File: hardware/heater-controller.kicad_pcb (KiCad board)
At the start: 2 copper layers, 65 x 63 mm, 12 parts, among them J1 Vitotronic plug 96, Q1 SFH 309 FA

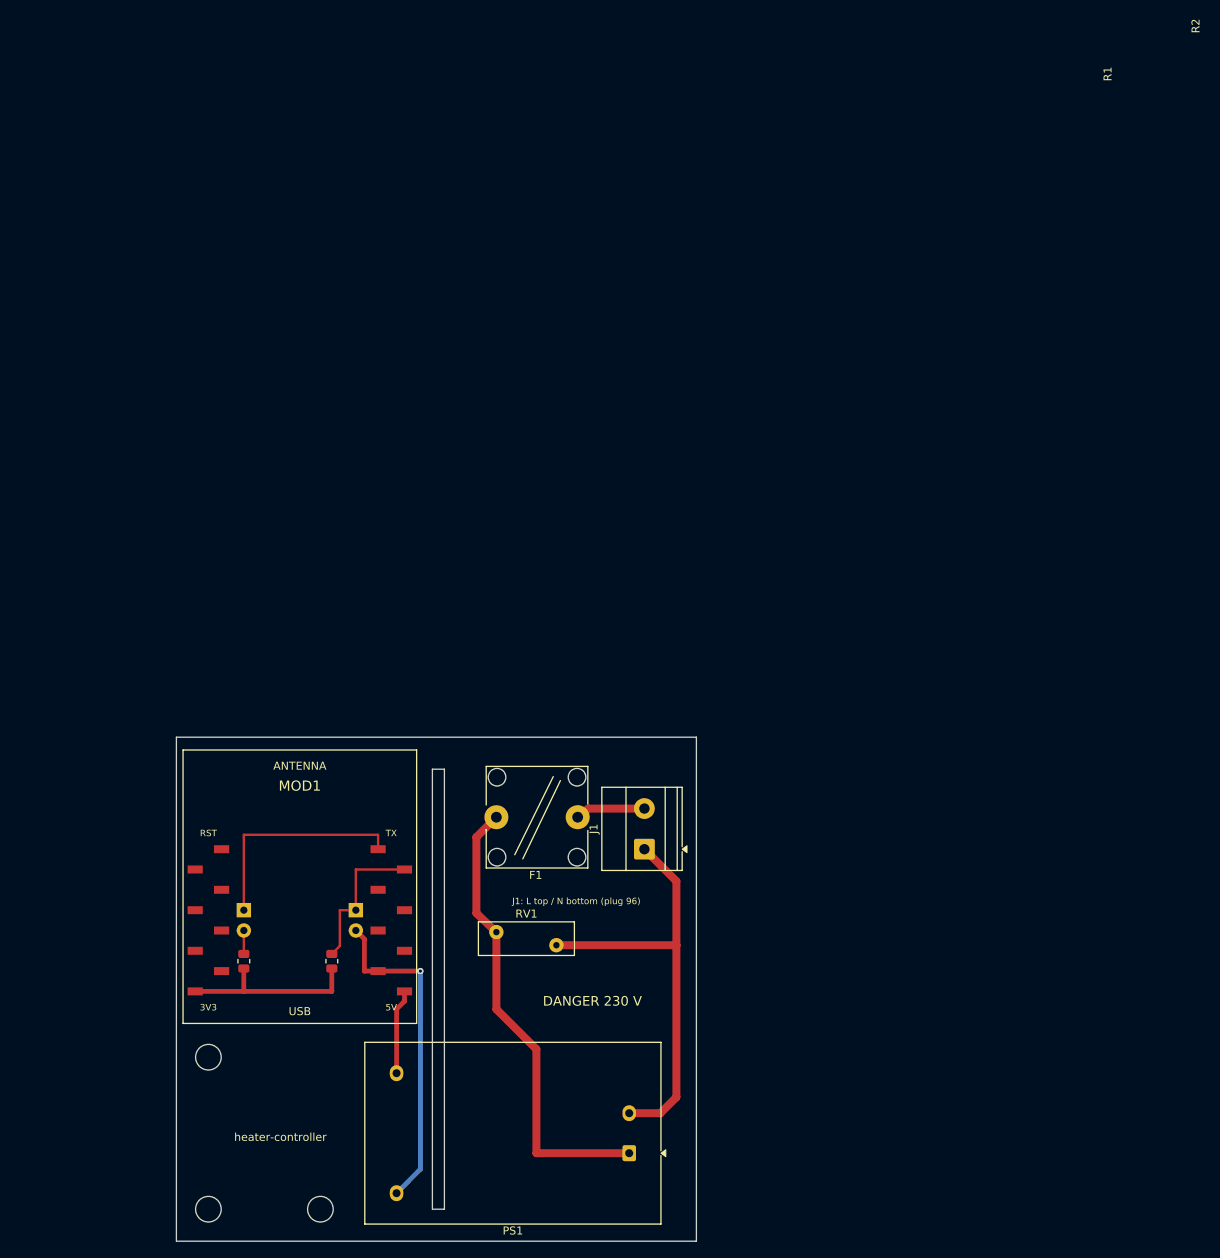
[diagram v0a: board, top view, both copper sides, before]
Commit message: feat(hardware): move to ESP32-C3 on a removable U-shaped board
- ESP32-C3 super mini replaces the D1 mini: Optolink UART on GPIO4/GPIO3,
  logs over native USB
- inverted U board (86 x 39.5 mm): 230 V leg, optical head header on the bar,
  C3 on SMD female sockets; screw terminal for the mains wires
- off-board optical head on a 4-wire ribbon
- back GND pour, 0.7 mm power tracks, 6 mm mains isolation checked by DRC
- C3 socket footprint generator and fabrication export script
- enclosure redrawn around the new board
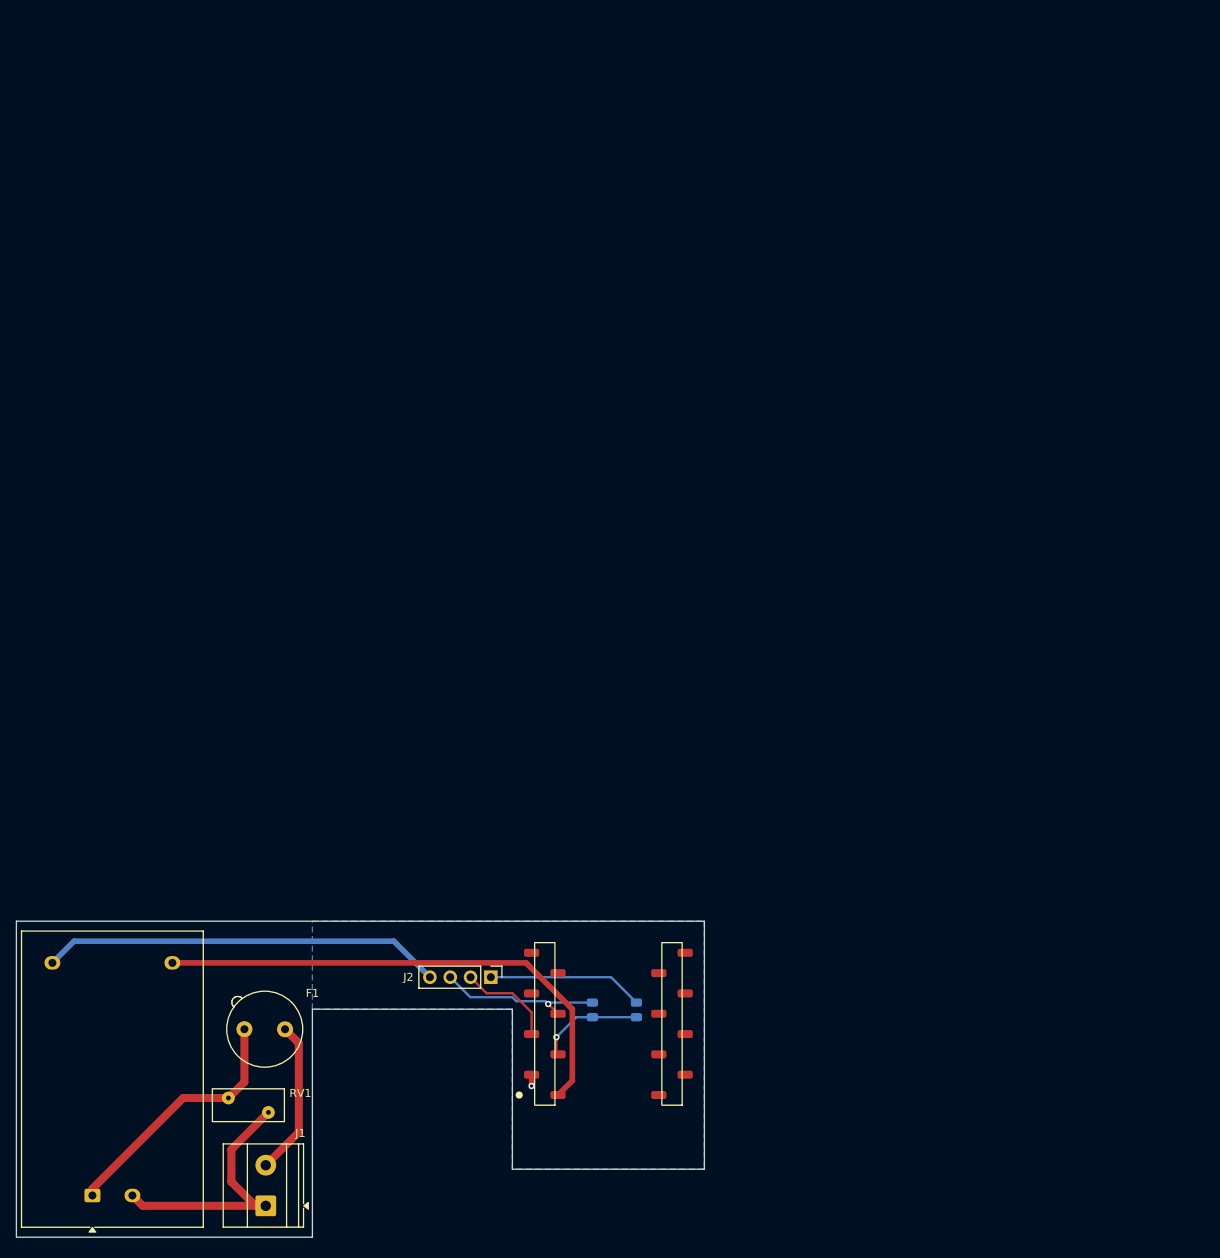
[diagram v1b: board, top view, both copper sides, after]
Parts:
- removed D1: SIR 204 EVL (IR), LED_THT:LED_D3.0mm_IRBlack
- removed H1, H2, H3: MountingHole_3.2mm_M3, MountingHole:MountingHole_3.2mm_M3
- removed Q1: SFH 309 FA, LED_THT:LED_D3.0mm_Clear
- added J2: Optical head, Connector_PinHeader_2.54mm:PinHeader_1x04_P2.54mm_Vertical, F.Cu at (139.3, 110.0)
- F1: value T500mA -> T500mA TR5; footprint Fuse:Fuseholder_Cylinder-5x20mm_Bulgin_FX0456_Vertical_Closed -> Fuse:Fuseholder_TR5_Littelfuse_No560_No460
- J1: value Vitotronic plug 96 -> Screw terminal (plug 96)
- MOD1: value WeMos_D1_mini -> ESP32-C3_SuperMini; footprint heater-controller:WEMOS_D1_mini_SMD_sockets -> heater-controller:ESP32-C3_SuperMini_Sockets
- R1, R2: moved to B.Cu
- RV1: value 10D561K -> 07D561K; footprint Varistor:RV_Disc_D12mm_W4.2mm_P7.5mm -> Varistor:RV_Disc_D9mm_W4.1mm_P5mm
- moved PS1 67.3 mm to (89.5, 137.3), turned to 90 degrees
- moved J1 65.0 mm to (111.2, 138.6)
- moved R1 49.4 mm to (157.5, 114.1)
- moved F1 45.2 mm to (113.6, 116.5)
- moved RV1 41.6 mm to (111.5, 126.9)
- moved MOD1 40.4 mm to (154.0, 115.0), turned to 180 degrees
- moved R2 33.1 mm to (152.0, 114.1)
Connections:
- MOD1 pad 1: unconnected-(MOD1-RST-Pad1) -> +5V
- MOD1 pad 10: /RX_GPIO3 -> unconnected-(MOD1-GPIO6-Pad10)
- MOD1 pad 15: GND -> unconnected-(MOD1-GPIO20/RX-Pad15)
- MOD1 pad 16: +5V -> unconnected-(MOD1-GPIO21/TX-Pad16)
- MOD1 pad 2: unconnected-(MOD1-A0-Pad2) -> GND
- MOD1 pad 3: unconnected-(MOD1-D0/GPIO16-Pad3) -> /3V3
- MOD1 pad 4: unconnected-(MOD1-D5/GPIO14-Pad4) -> /TX_GPIO4
- MOD1 pad 5: unconnected-(MOD1-D6/GPIO12-Pad5) -> /RX_GPIO3
- MOD1 pad 8: /3V3 -> unconnected-(MOD1-GPIO0-Pad8)
- MOD1 pad 9: /TX_GPIO1 -> unconnected-(MOD1-GPIO5-Pad9)
- R1 pad 2: Net-(D1-A) -> /LED_A
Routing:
- net +5V: track 10.6 -> 63.9 mm
- net /TX_GPIO1: track 28.0 -> 0.00 mm
- net /L_FUSED: track 57.8 -> 32.0 mm
- net /N: track 54.4 -> 33.3 mm
- net /LED_A: track 0.00 -> 19.5 mm
- net /TX_GPIO4: track 0.00 -> 12.2 mm
- net /L: track 8.72 -> 19.4 mm
- net GND: track 41.5 -> 51.6 mm
- net /3V3: track 22.8 -> 13.3 mm, vias 0 -> 1
- net Net-(D1-A): track 2.93 -> 0.00 mm
- net /RX_GPIO3: track 19.0 -> 21.0 mm, vias 0 -> 1
- added copper zone on B.Cu, net GND
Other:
- board size 65 x 63 mm -> 86 x 39.5 mm
- board text removed: "DANGER 230 V"
- board text removed: "J1: L top / N bottom (plug 96)"
- board text removed: "OPTOLINK"
- board text removed: "RX"
- board text removed: "TX (IR LED)"
- board text removed: "heater-controller"

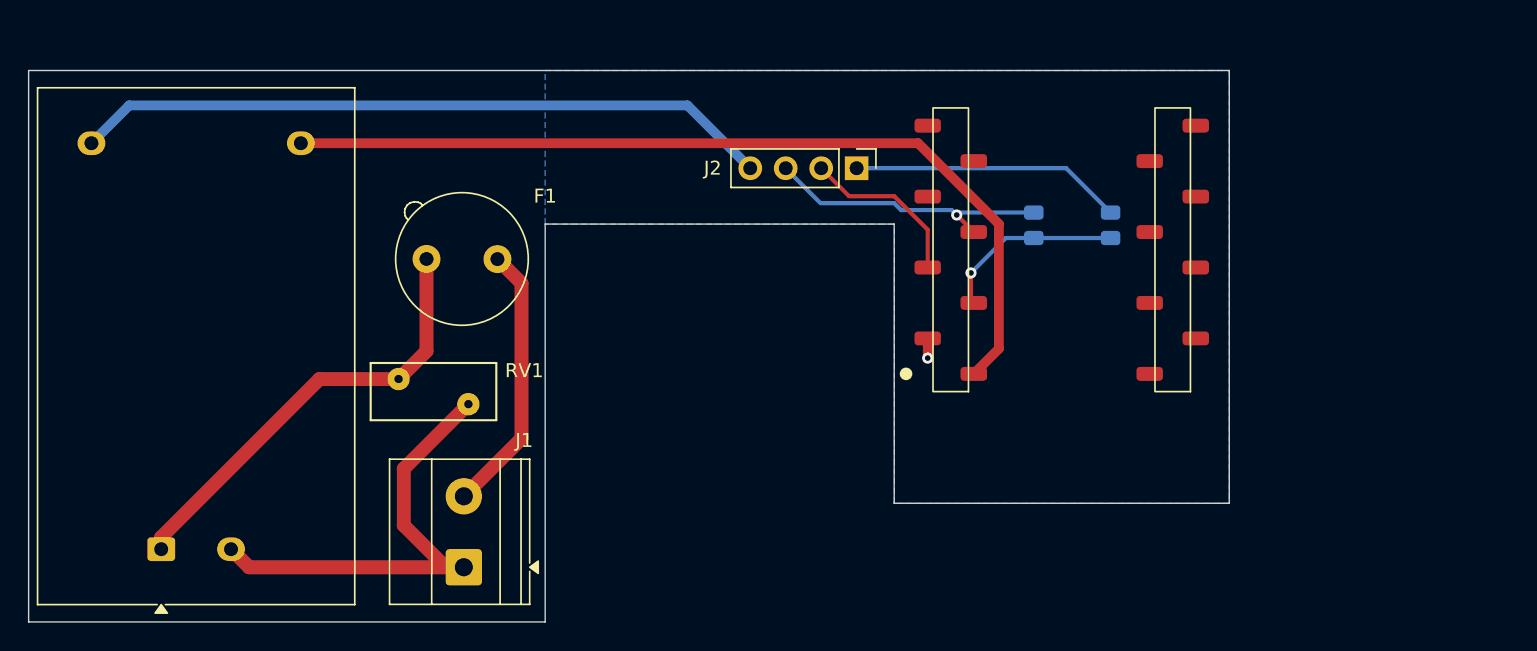
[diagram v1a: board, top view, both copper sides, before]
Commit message: feat(hardware): hand-solderable board with SMD C3 sockets for JLCPCB
- C3 plugged into two hanxia 1x8 SMD sockets (J3/J4) at 15.24 mm, the only
  parts with an LCSC number; MOD1 off board with a board-only outline
- through-hole everything else: TR5 T1A fuse, 07D431K varistor, JST PH
  vertical optical head connector, axial resistors
- HLK-PM01 footprint from the Hi-Link datasheet (15.4 / 29.4 mm pin pitch)
- footprints generated by footprints.py from the datasheets
- export adds the JLCPCB BOM and placement files
- routing done in KiCad: 0.7 mm power tracks, no ground plane
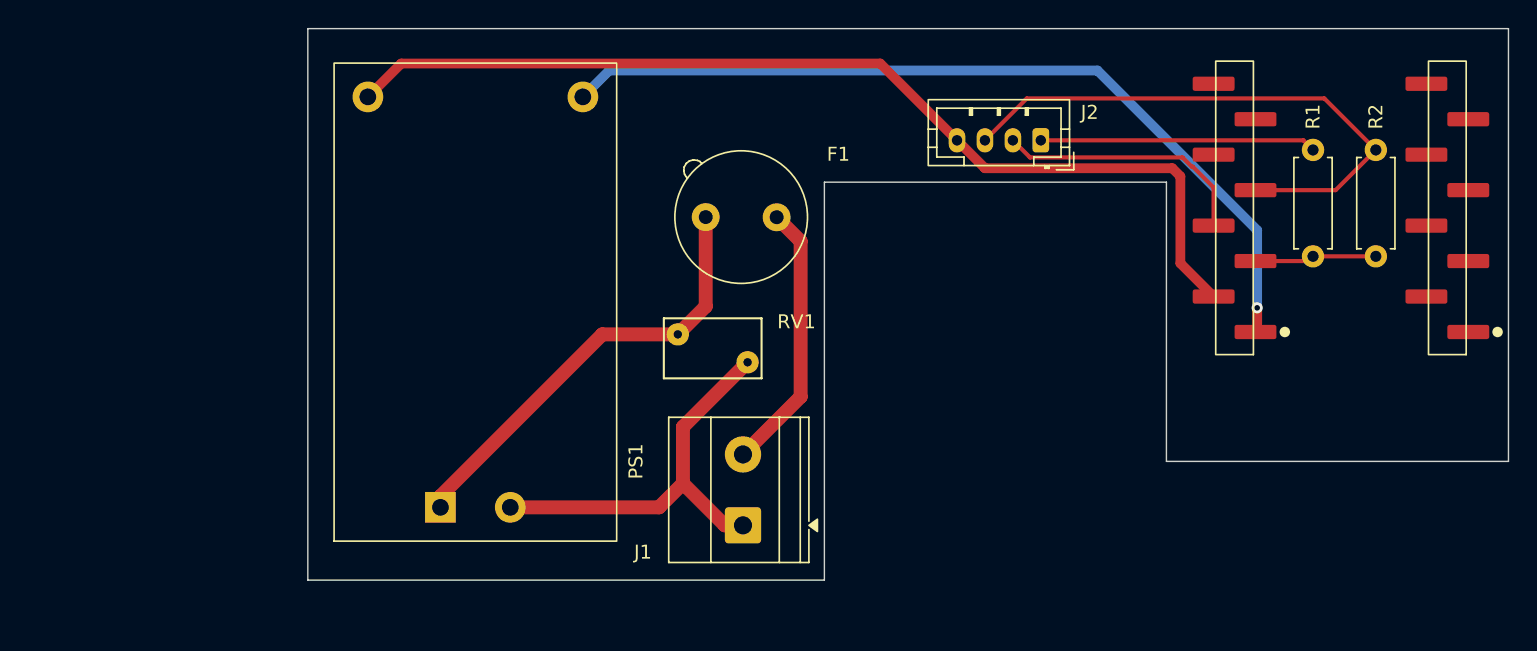
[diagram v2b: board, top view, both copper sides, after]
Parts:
- added J3: Socket 1x8 SMD (C3 pins 1-8), heater-controller:PinSocket_1x08_P2.54mm_SMD_HX-ZQ, F.Cu at (166.4, 112.8)
- added J4: Socket 1x8 SMD (C3 pins 9-16), heater-controller:PinSocket_1x08_P2.54mm_SMD_HX-ZQ, F.Cu at (181.6, 112.8)
- F1: value T500mA TR5 -> T1A TR5
- J2: value Optical head -> Optical head JST PH 4P; footprint Connector_PinHeader_2.54mm:PinHeader_1x04_P2.54mm_Vertical -> Connector_JST:JST_PH_B4B-PH-K_1x04_P2.00mm_Vertical
- MOD1: footprint heater-controller:ESP32-C3_SuperMini_Sockets -> heater-controller:ESP32-C3_SuperMini_Outline
- PS1: footprint Converter_ACDC:Converter_ACDC_Hi-Link_HLK-PMxx -> heater-controller:Converter_ACDC_HLK-PM01
- R1, R2: footprint Resistor_SMD:R_0805_2012Metric -> Resistor_THT:R_Axial_DIN0207_L6.3mm_D2.5mm_P7.62mm_Horizontal; moved to F.Cu
- RV1: value 07D561K -> 07D431K (275VAC); footprint Varistor:RV_Disc_D9mm_W4.1mm_P5mm -> Varistor:RV_Disc_D7mm_W4.3mm_P5mm
- moved R2 24.6 mm to (176.5, 116.3)
- moved MOD1 20.2 mm to (174.0, 112.0)
- moved RV1 20.2 mm to (131.5, 123.9)
- moved F1 20.2 mm to (133.6, 113.5)
- moved PS1 20.2 mm to (109.5, 134.3)
- moved J1 20.2 mm to (131.2, 135.6)
- moved R1 14.7 mm to (172.0, 116.3)
- moved J2 13.3 mm to (152.5, 108.0), turned to 180 degrees
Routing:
- net GND: track 51.6 -> 72.1 mm, vias 1 -> 0
- net /RX_GPIO3: track 21.0 -> 40.6 mm, vias 1 -> 0
- net /TX_GPIO4: track 12.2 -> 18.7 mm
- net /3V3: track 13.3 -> 8.76 mm, vias 1 -> 0
- net /N: track 33.3 -> 29.2 mm
- net +5V: track 63.9 -> 61.0 mm, vias 0 -> 1
- removed copper zone on B.Cu, net GND
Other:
- outline, holes or cut-outs redrawn

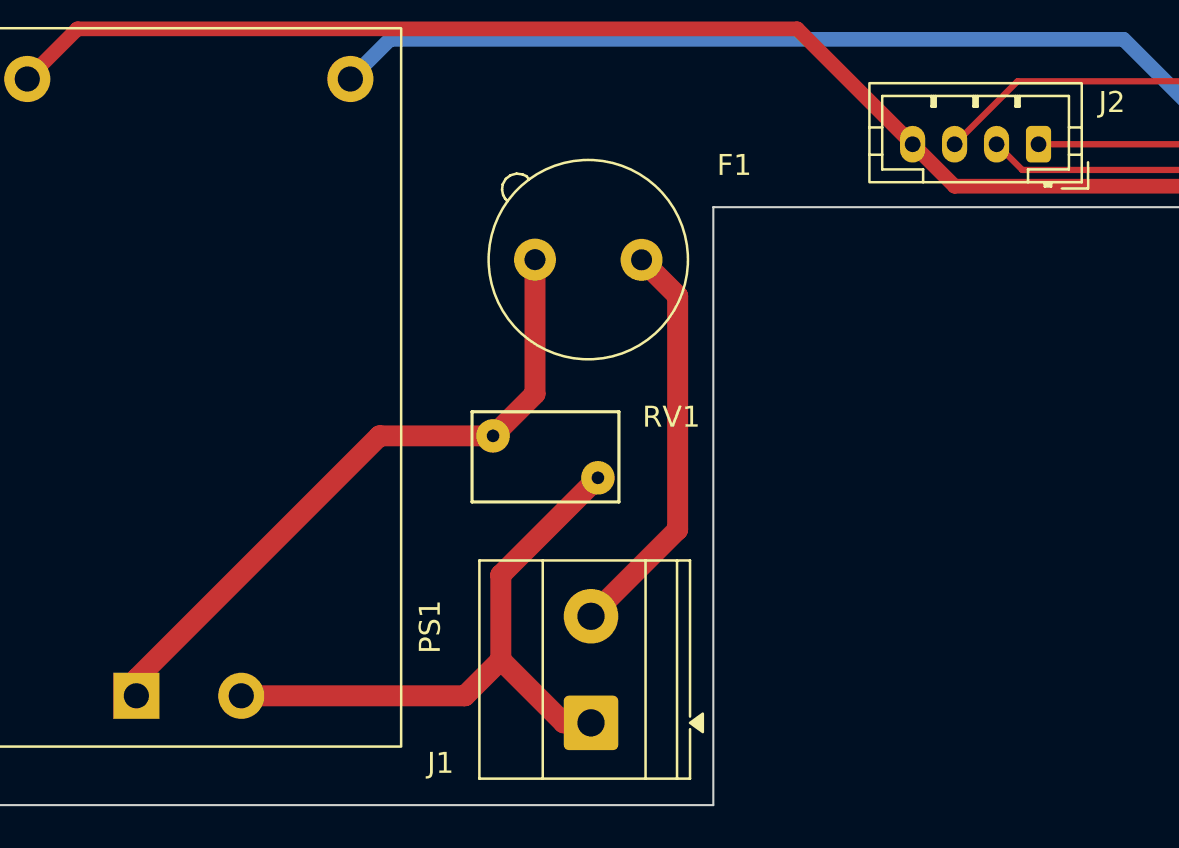
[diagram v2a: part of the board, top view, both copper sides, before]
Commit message: feat(hardware): source every part at LCSC with datasheet footprints
- Kefa KF128 terminal block (Phoenix MKDS out of stock), Bourns MOV-07D431K
  inline varistor and JST PH with 0.9 mm holes, drawn by footprints.py
- LCSC number on every part; split-bom.py writes the JLCPCB BOM (SMD only)
  and an LCSC cart for the hand-soldered parts
- RV1 rerouted for its inline leads; DRC clean, schematic parity
- Enclosure split into named bodies: shells, lid, optical plug
- READMEs: parts list with suppliers, prices and footprint specs
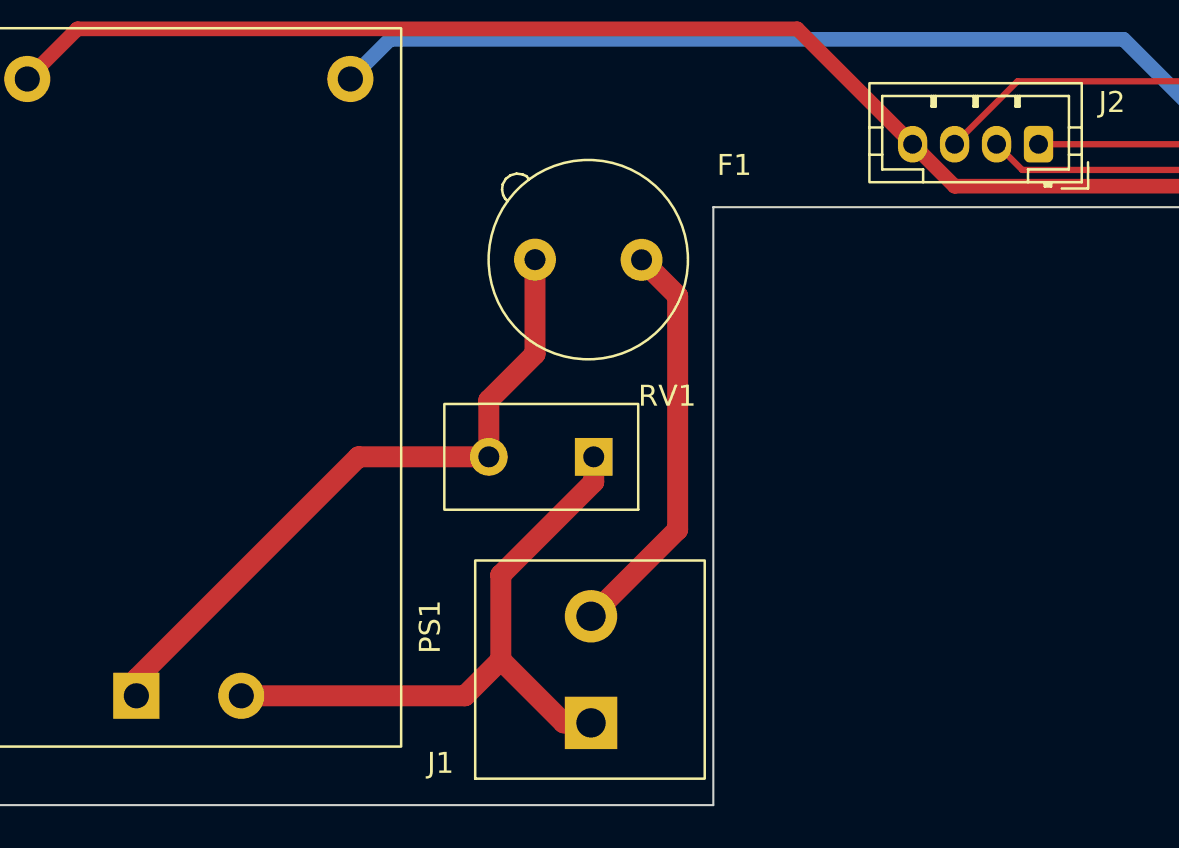
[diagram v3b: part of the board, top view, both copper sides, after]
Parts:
- F1: value T1A TR5 -> TR5 holder + T1A fuse
- J1: value Screw terminal (plug 96) -> KF128-5.08 (plug 96); footprint TerminalBlock_Phoenix:TerminalBlock_Phoenix_MKDS-1,5-2-5.08_1x02_P5.08mm_Horizontal -> heater-controller:TerminalBlock_Kefa_KF128-5.08_1x02
- J2: value Optical head JST PH 4P -> JST B4B-PH-K (optical head); footprint Connector_JST:JST_PH_B4B-PH-K_1x04_P2.00mm_Vertical -> heater-controller:JST_PH_B4B-PH-K_1x04_P2.00mm_Vertical_Drill0.9
- RV1: value 07D431K (275VAC) -> MOV-07D431K (275VAC); footprint Varistor:RV_Disc_D7mm_W4.3mm_P5mm -> heater-controller:RV_Disc_D9mm_W4.8mm_P5mm_Inline
- moved RV1 1.02 mm to (131.3, 122.9)
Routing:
- net /N: track 29.2 -> 30.1 mm
